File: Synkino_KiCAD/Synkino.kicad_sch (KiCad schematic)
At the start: 161 parts, among them J1 Pwr, J10 EYE8_OUT, J11 EYE4_OUT, J12 2.5mm, J13 EYE5_OUT, J2 2.5mm, J3 3.5mm, J4 Micro_SD_Card_Det_Hirose_DM3AT, J5 EYE1_OUT, J6 EYE6_OUT, J7 EYE2_OUT, J8 EYE7_OUT, J9 EYE3_OUT, Q1 IRF7319, Q2 BC847, Q3 IRLML2244 o. AO3401A, SW1 SW_Push, SW2 Rotary_Encoder_Switch, SW3 SW_Push, U1 MCP1702T-5002E/MB, U10 ATMEGA328P-AU, U11 QRE1113, U12 QRE1113, U13 QRE1113, U14 QRE1113, U15 QRE1113, U16 QRE1113, U17 24LC256, U18 QRE1113, U2 ATMEGA328P-AU, U3 74HC4050, U4 SPIOLED128x64, U5 AP7312-1833W6-7, U6 74HC14, U7 VS1053B, U8 MAX4741, U9 QRE1113, X1 FTDIconn, X2 ICSP, X3 FTDIconn, X4 ICSP, Y1 16Mhz, Y2 12.288MHz, Y3 16Mhz

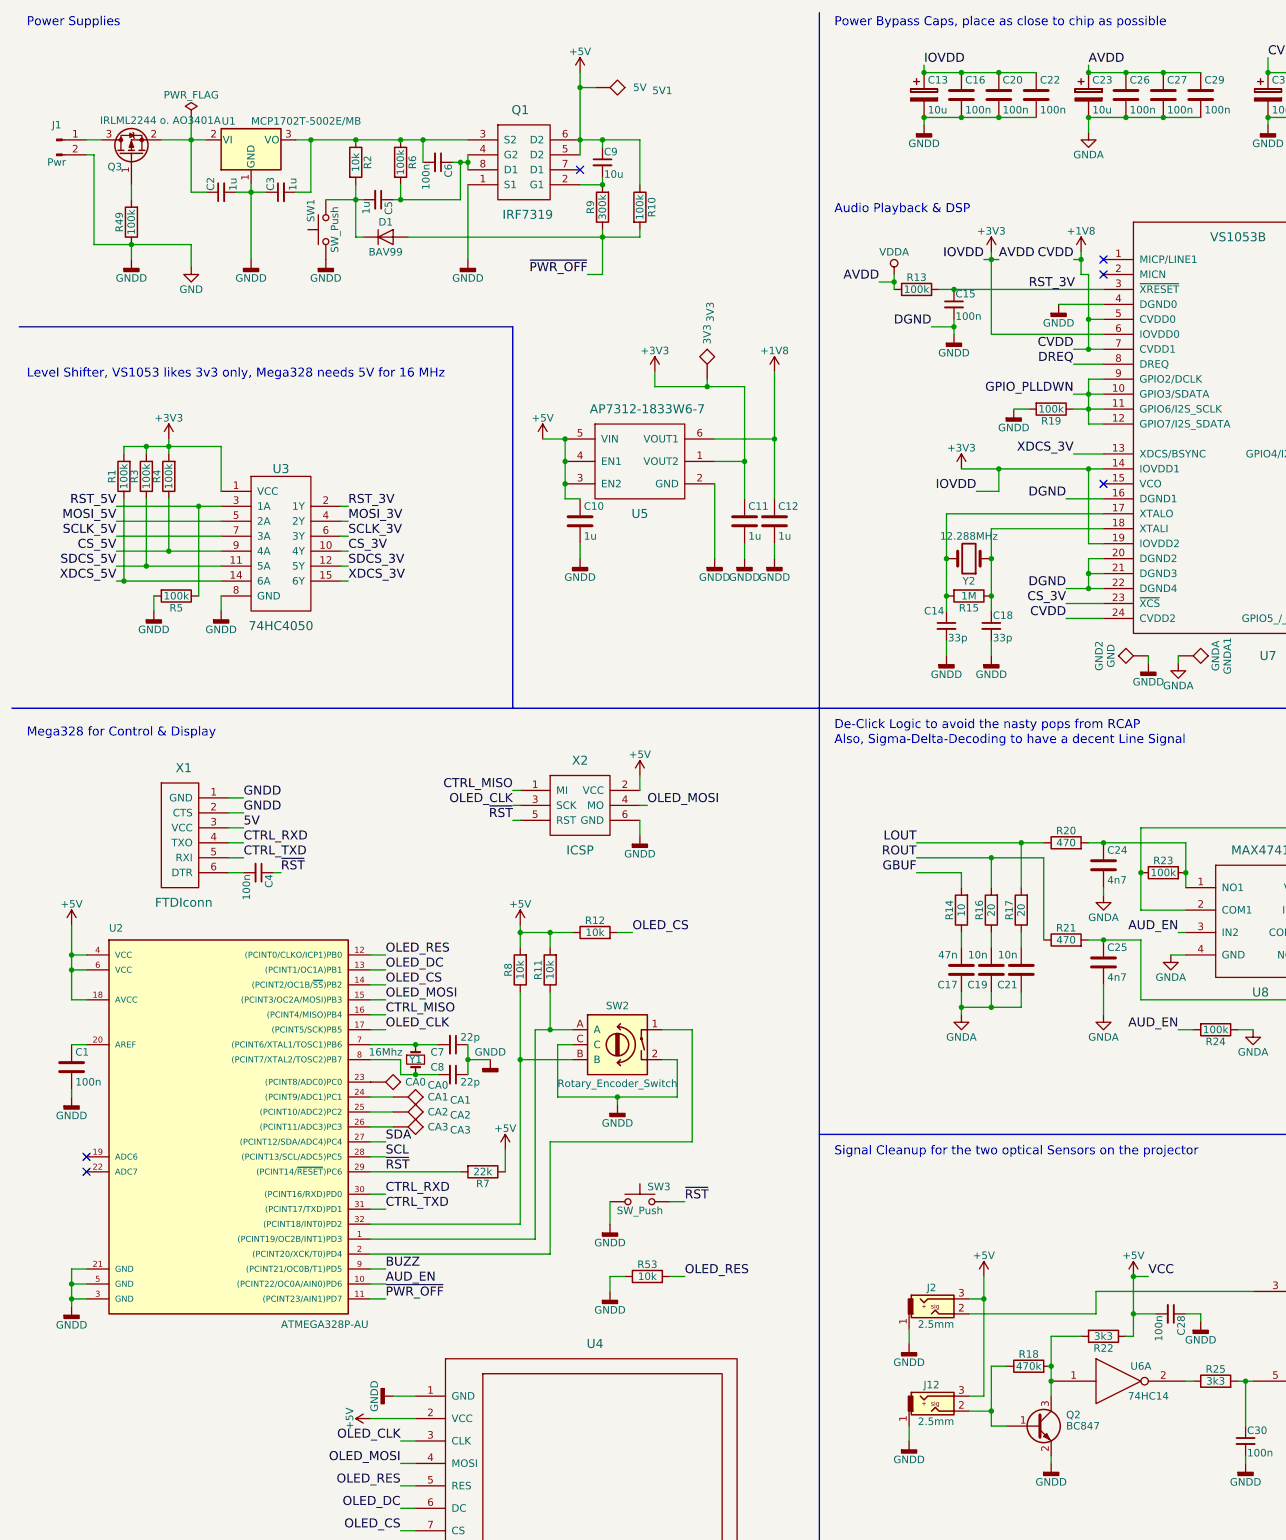
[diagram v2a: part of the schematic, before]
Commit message: Eyes flattr (0402), wider 1.8V net, D7 gone, more SMTA prep
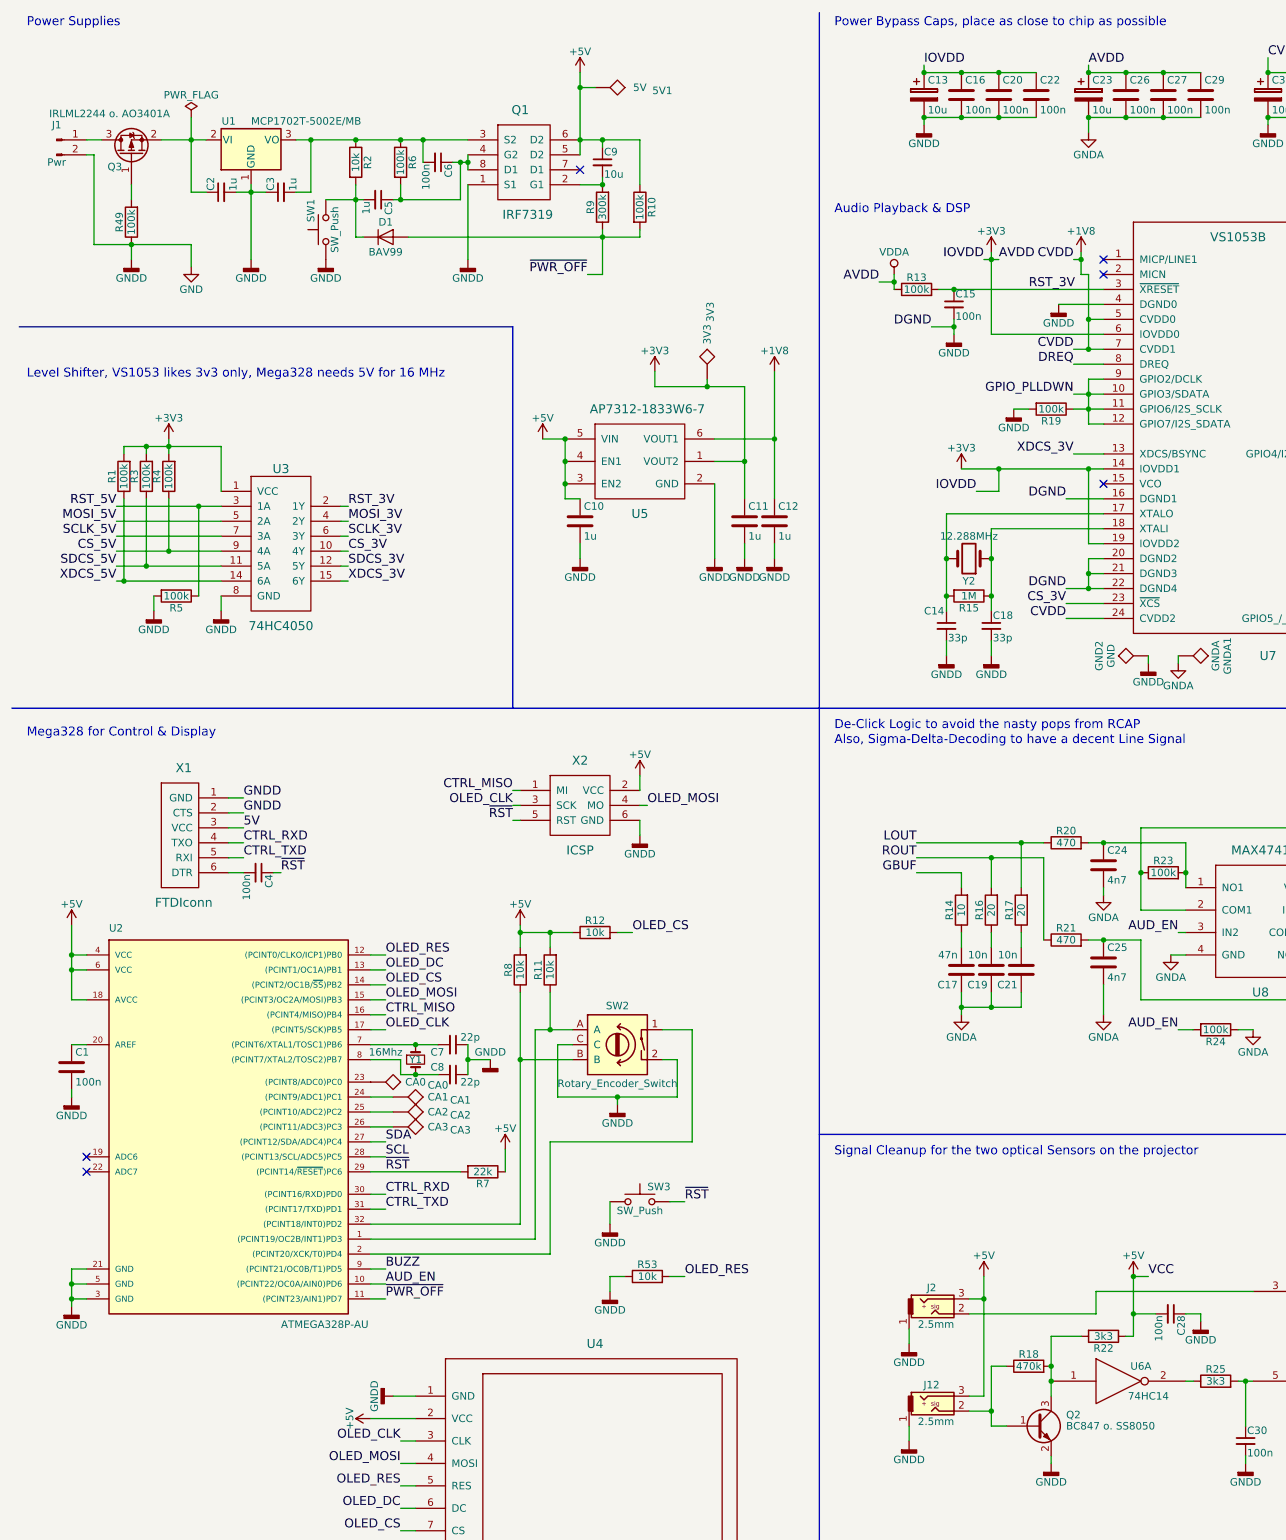
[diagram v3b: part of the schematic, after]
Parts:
- 3V3, 5V1, AA0, AA1, AA2, AA3, AD10, AD4, CA0, CA1, CA2, CA3, GND1, GND2, GNDA1, J1, J10, J11, J13, J5, J6, J7, J8, J9, SCL1, SDA1, X1, X2, X3, X4: Inventory (none) -> -
- BZ1, J12, J2, J3, J4, Q1, SW1, SW2, SW3, U1, U10, U11, U12, U13, U14, U15, U16, U17, U18, U2, U3, U4, U5, U7, U8, U9, Y1, Y2, Y3: Inventory (none) -> L
- Q2: value BC847 -> BC847 o. SS8050; Inventory (none) -> B; LCSC (none) -> C2150
- R1, R10, R13, R19, R23, R24, R26, R27, R28, R29, R3, R4, R49, R5, R6: Inventory (none) -> B; LCSC (none) -> C149504
- R11, R12, R2, R35, R36, R53, R8: Inventory (none) -> B; LCSC (none) -> C17414
- R14: Inventory (none) -> B; LCSC (none) -> C17415
- R15: Inventory (none) -> B; LCSC (none) -> C17514
- R16, R17: Inventory (none) -> B; LCSC (none) -> C17544
- R18: Inventory (none) -> B; LCSC (none) -> C17709
- R20, R21: Inventory (none) -> B; LCSC (none) -> C17710
- R22, R25: Inventory (none) -> B; LCSC (none) -> C26010
- R30, R47: Inventory (none) -> B; LCSC (none) -> C17798
- R31, R32, R33, R40, R42, R43, R46, R50: footprint Resistor_SMD:R_0805_2012Metric -> Resistor_SMD:R_0402_1005Metric; Inventory (none) -> B; LCSC (none) -> C25091
- R34, R38, R39, R41, R44, R45, R48, R52: footprint Resistor_SMD:R_0805_2012Metric -> Resistor_SMD:R_0402_1005Metric; Inventory (none) -> B; LCSC (none) -> C25792
- R37, R7: Inventory (none) -> B; LCSC (none) -> C17560
- R51: Inventory (none) -> B; LCSC (none) -> C17408
- R9: footprint Resistor_SMD:R_0805_2012Metric -> Resistor_SMD:R_0603_1608Metric; Inventory (none) -> B; LCSC (none) -> C23024
- U6: Inventory (none) -> B; LCSC (none) -> C5605

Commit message: Footprints updated to newer KiCad and SMTA versions
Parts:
- 3V3, 5V1: footprint Measurement_Points:Measurement_Point_Round-TH_Small -> TestPoint:TestPoint_Pad_1.5x1.5mm
- AA0, AA1, AA2, AA3, AD10, AD4, GND1, SCL1, SDA1: footprint Measurement_Points:Measurement_Point_Round-TH_Small -> TestPoint:TestPoint_THTPad_1.5x1.5mm_Drill0.7mm
- C1, C10, C11, C12, C14, C15, C16, C17, C18, C19, C2, C20, C21, C22, C24, C25, C26, C27, C28, C29, C3, C30, C32, C33, C34, C37, C38, C39, C4, C41, C42, C43, C5, C6, C7, C8, C9: footprint Capacitors_SMD:C_0805_HandSoldering -> Capacitor_SMD:C_0805_2012Metric
- CA0, CA1, CA2, CA3: footprint Measurement_Points:Measurement_Point_Round-TH_Small -> TestPoint:TestPoint_THTPad_D1.5mm_Drill0.7mm
- D1: footprint Diodes_SMD:D_SOT-23_NKA -> easyeda2kicad:SOT-23-3_L2.9-W1.3-P1.90-LS2.4-BR
- GND2, GNDA1: footprint Measurement_Points:Measurement_Point_Square-SMD-Pad_Small -> TestPoint:TestPoint_Pad_2.0x2.0mm
- J1: footprint Connectors_Molex:Molex_KK-6410-02_02x2.54mm_Straight -> Connector_PinHeader_2.54mm:PinHeader_1x02_P2.54mm_Horizontal
- J10, J11, J13, J5, J6, J7, J8, J9: footprint Pin_Headers:Pin_Header_Straight_1x03_Pitch2.54mm -> Connector_PinSocket_2.54mm:PinSocket_1x03_P2.54mm_Vertical
- Q1, U17: footprint Housings_SOIC:SOIC-8_3.9x4.9mm_Pitch1.27mm -> Package_SO:SOIC-8_3.9x4.9mm_P1.27mm
- SW1: footprint Buttons_Switches_THT:SW_PUSH_6mm_h5mm -> easyeda2kicad:KEY-TH_4P-L12.0-W12.0-P5.0-LS12.5-EH-small
- SW3: footprint Buttons_Switches_THT:SW_PUSH_6mm_h5mm -> easyeda2kicad:SW-SMD_4P-L5.1-W5.1-P3.70-LS6.5-TL-2
- U1: footprint TO_SOT_Packages_SMD:SOT-89-3_Handsoldering -> Package_TO_SOT_SMD:SOT-89-3
- U10, U2: footprint Housings_QFP:TQFP-32_7x7mm_Pitch0.8mm -> Package_QFP:TQFP-32_7x7mm_P0.8mm
- U3: footprint Housings_SOIC:SOIC-16_3.9x9.9mm_Pitch1.27mm -> Package_SO:SOIC-16_3.9x9.9mm_P1.27mm
- U6: footprint Housings_SOIC:SOIC-14_3.9x8.7mm_Pitch1.27mm -> Package_SO:SOIC-14_3.9x8.7mm_P1.27mm
- U7: footprint Housings_QFP:LQFP-48_7x7mm_Pitch0.5mm -> Package_QFP:LQFP-48_7x7mm_P0.5mm
- U8: footprint Housings_SSOP:MSOP-8_3x3mm_Pitch0.65mm -> Package_SO:MSOP-8_3x3mm_P0.65mm
- X1, X3: footprint Pin_Headers:Pin_Header_Straight_1x06_Pitch2.54mm -> Connector_PinSocket_2.54mm:PinSocket_1x06_P2.54mm_Vertical
- X2, X4: footprint Pin_Headers:Pin_Header_Straight_2x03_Pitch2.54mm -> Connector_PinSocket_2.54mm:PinSocket_2x03_P2.54mm_Vertical
